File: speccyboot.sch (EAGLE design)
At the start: 15 parts, among them IC1 74HCT139N, IC2 74HCT273N, IC3 28C64, IC4 7432N, IC5 74HCT244N, IC6 5V REG, IC7 3.3V REG

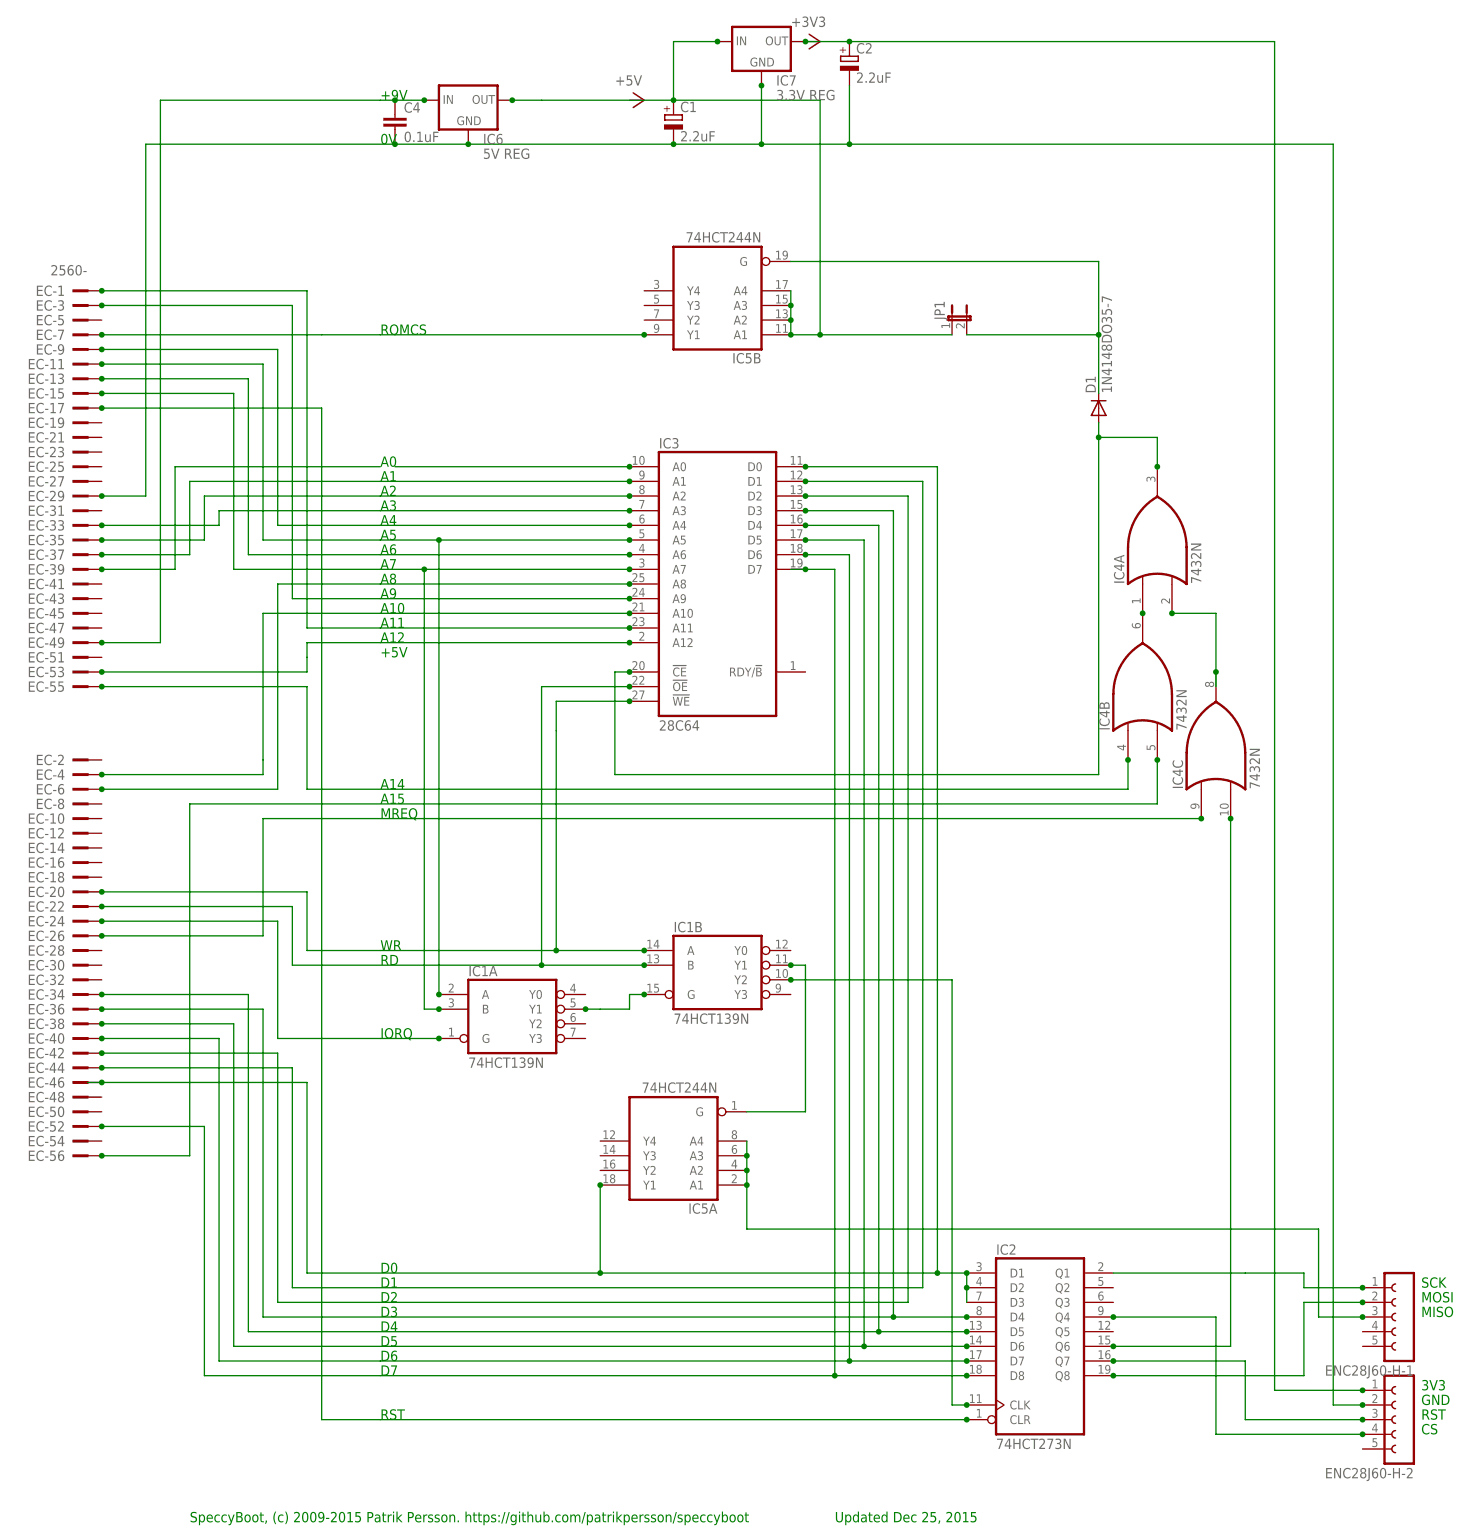
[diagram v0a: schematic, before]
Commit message: updated schematics
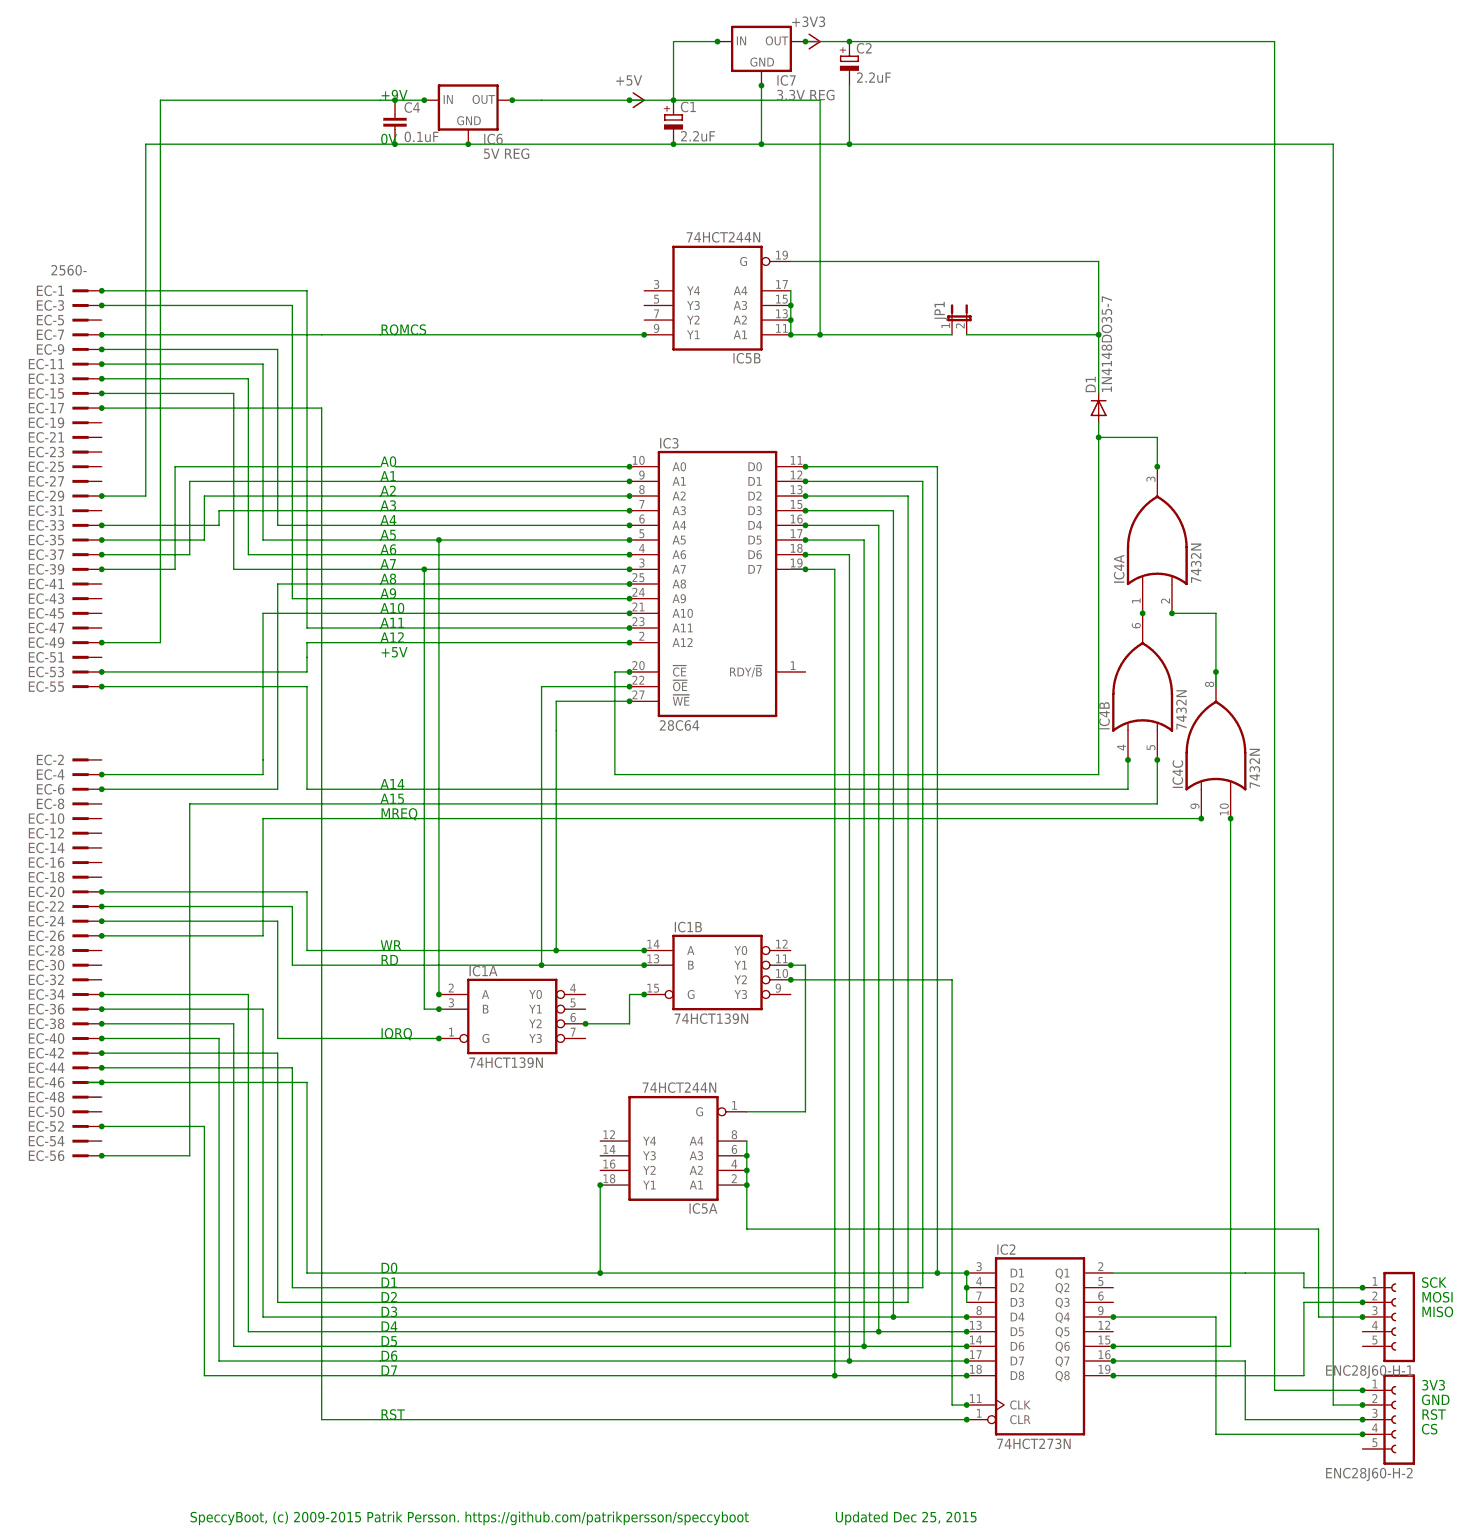
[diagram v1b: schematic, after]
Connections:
- removed net N$11: IC1A.Y1, IC1B.G
- new net N$34: IC1A.Y2, IC1B.G
- net N$3: now also IC4C.O

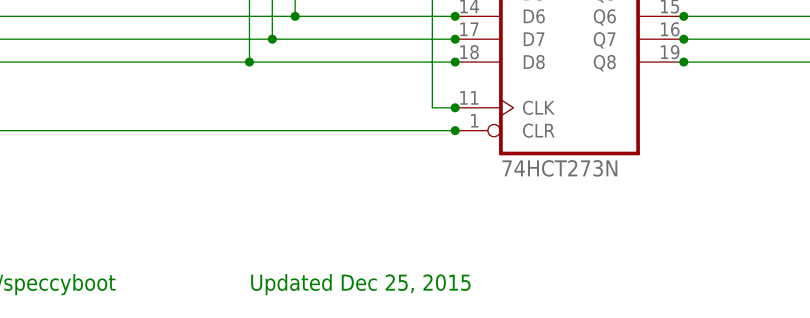
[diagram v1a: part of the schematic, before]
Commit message: date adjusted in schematic
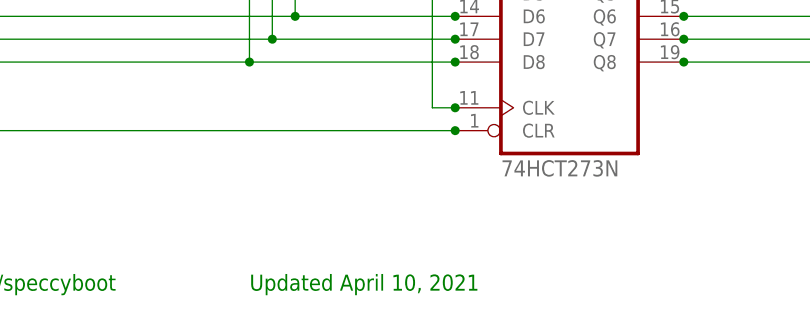
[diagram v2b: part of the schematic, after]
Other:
- note added: "Updated April 10, 2021"
- note removed: "Updated Dec 25, 2015"
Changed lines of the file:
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@@
 <text x="170.18" y="-40.64" size="1.778" layer="91">RST</text>
 <text x="170.18" y="-43.18" size="1.778" layer="91">CS</text>
-<text x="68.58" y="-58.42" size="1.778" layer="91">Updated Dec 25, 2015</text>
+<text x="68.58" y="-58.42" size="1.778" layer="91">Updated April 10, 2021</text>
 </plain>
 <instances>

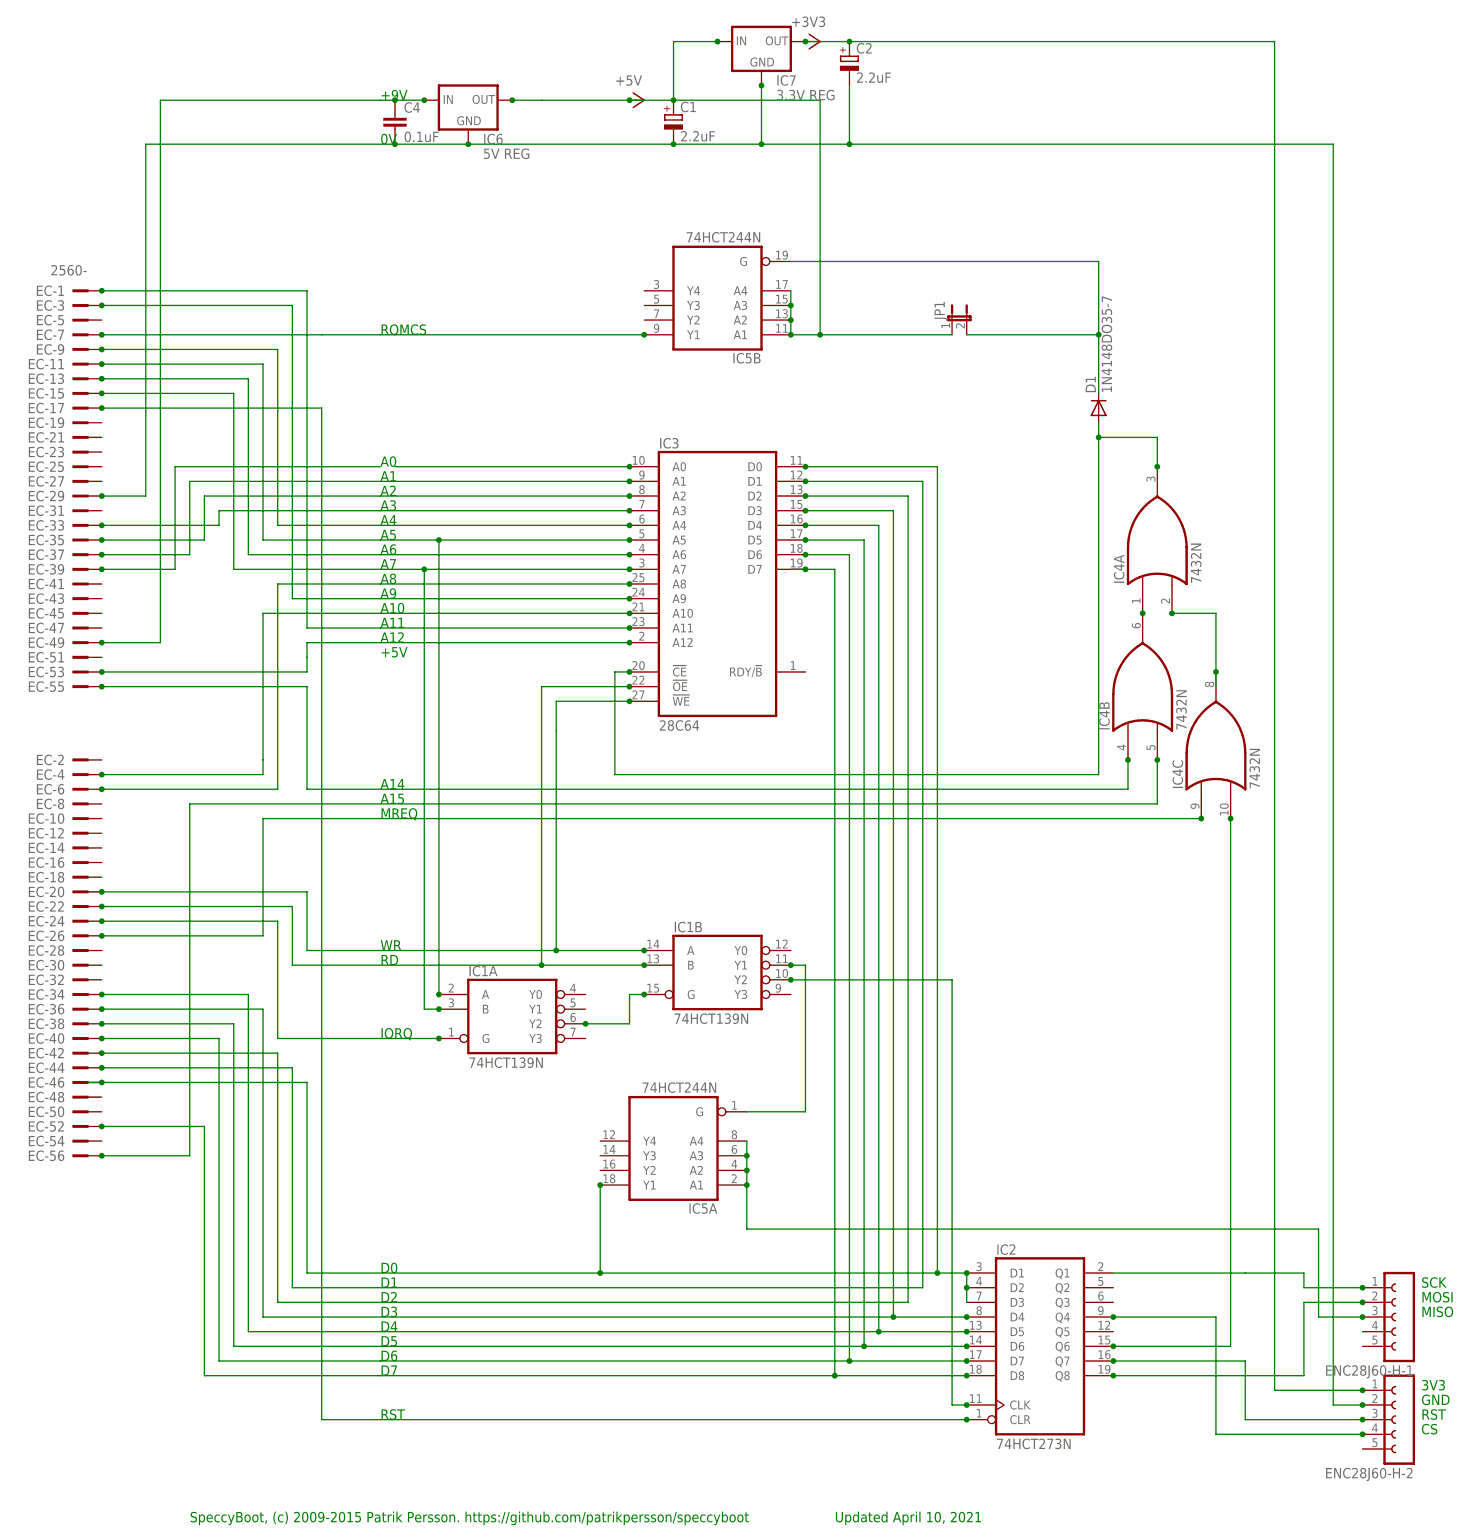
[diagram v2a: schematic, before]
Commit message: doc update for version 3
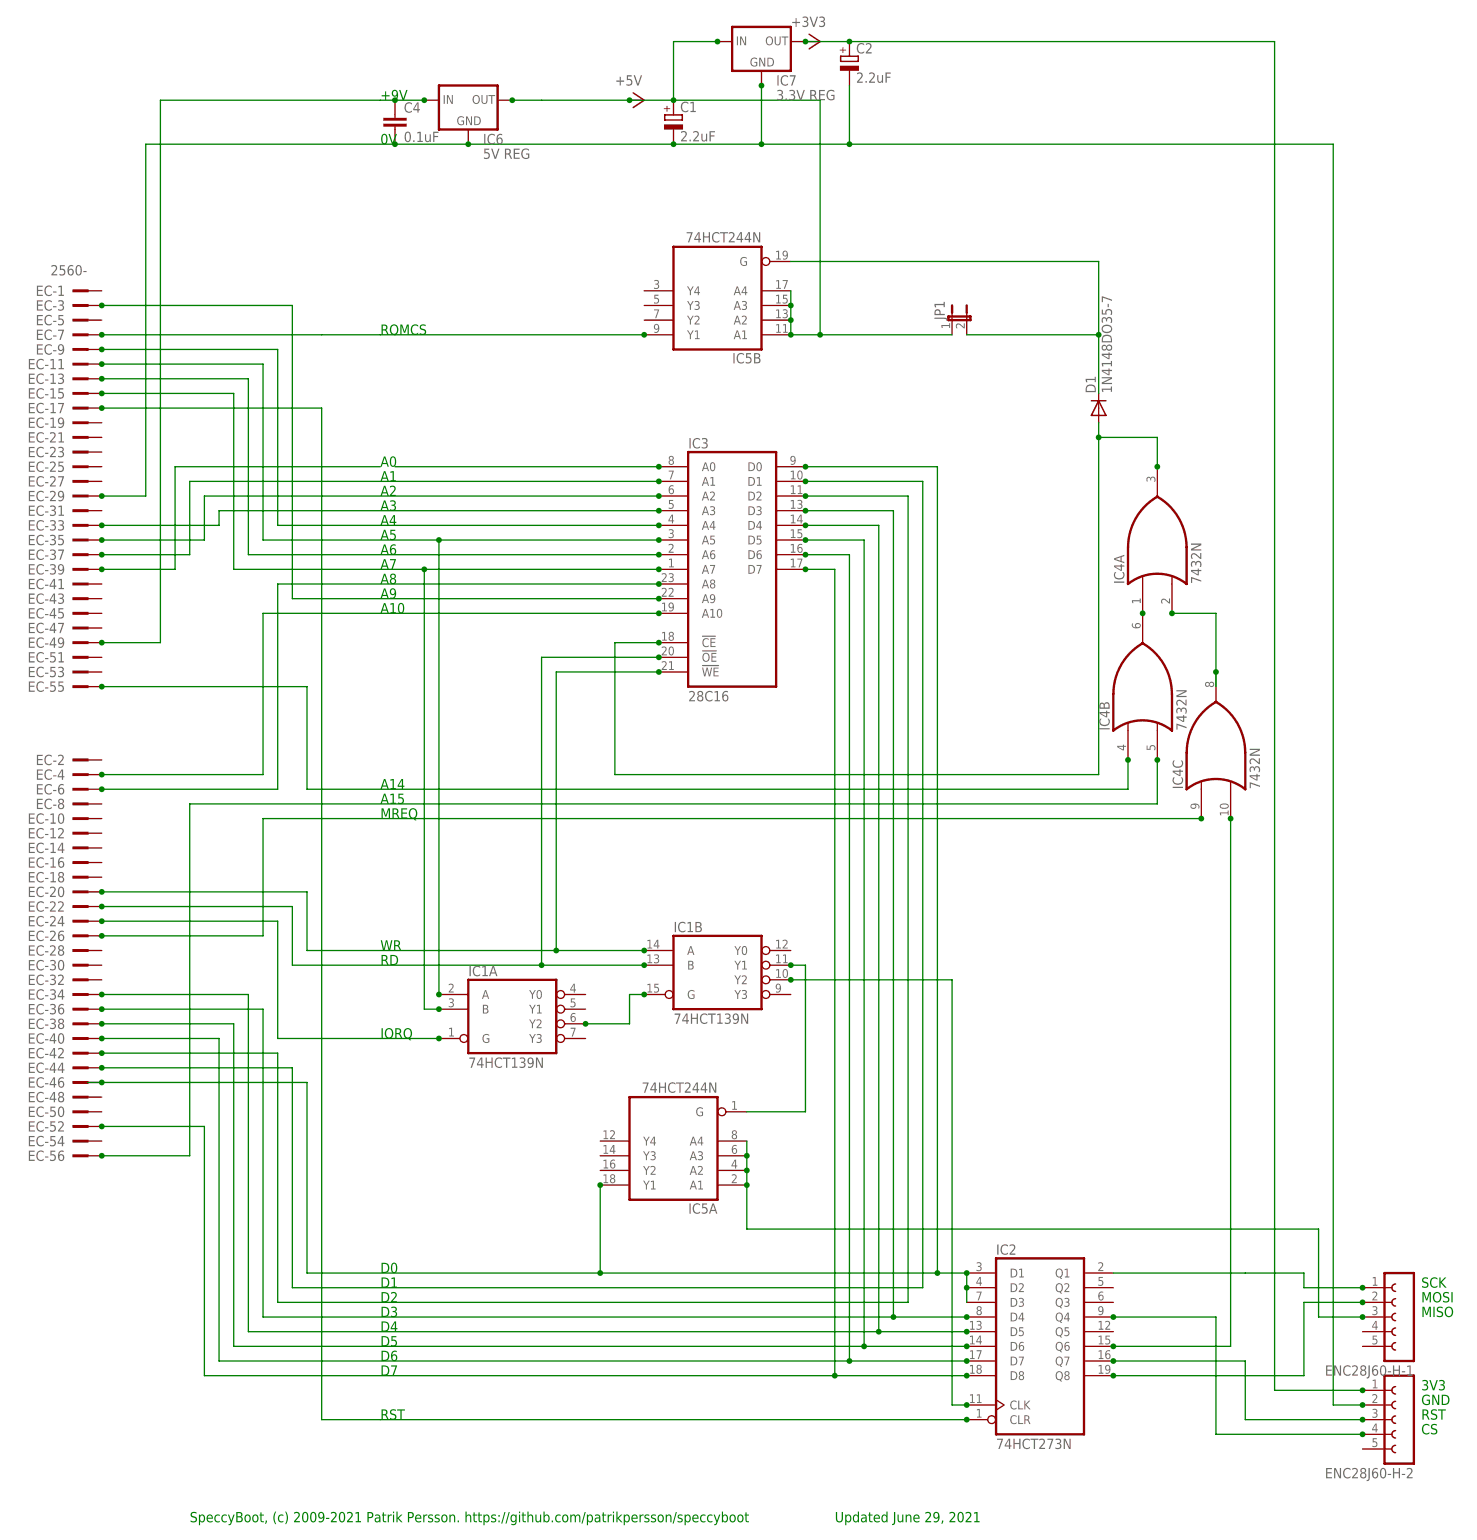
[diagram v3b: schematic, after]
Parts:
- IC3: value 28C64 -> 28C16; device memory:2864 -> memory:2816
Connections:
- removed net N$28: EC-1.KL, IC3A.A11
- removed net N$29: EC-53.KL, IC3A.A12
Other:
- note added: "SpeccyBoot, (c) 2009-2021 Patrik Persson. https://github.com/patrikpersson/speccyboot"
- note added: "Updated June 29, 2021"
- note removed: "+5V"
- note removed: "A11"
- note removed: "A12"
- note removed: "SpeccyBoot, (c) 2009-2015 Patrik Persson. https://github.com/patrikpersson/speccyboot"
- note removed: "Updated April 10, 2021"
